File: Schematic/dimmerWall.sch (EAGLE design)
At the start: 22 parts, among them Q1 IRF840, T1 BC547

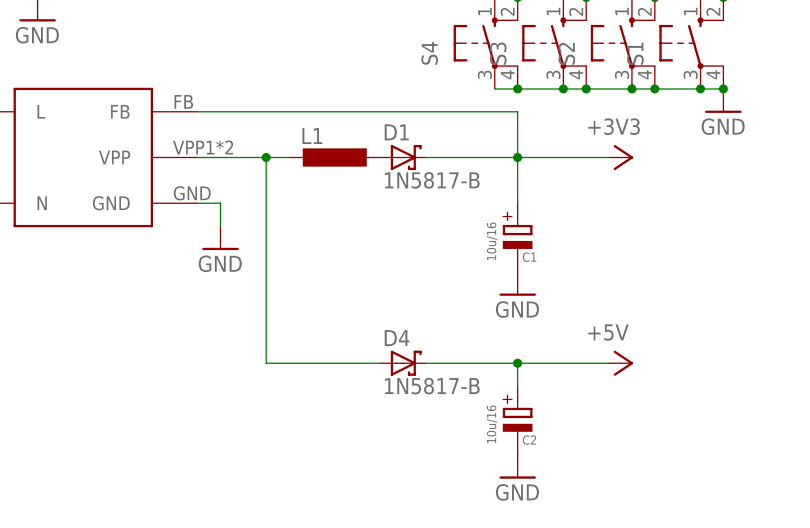
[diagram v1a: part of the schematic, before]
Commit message: Add L dimension
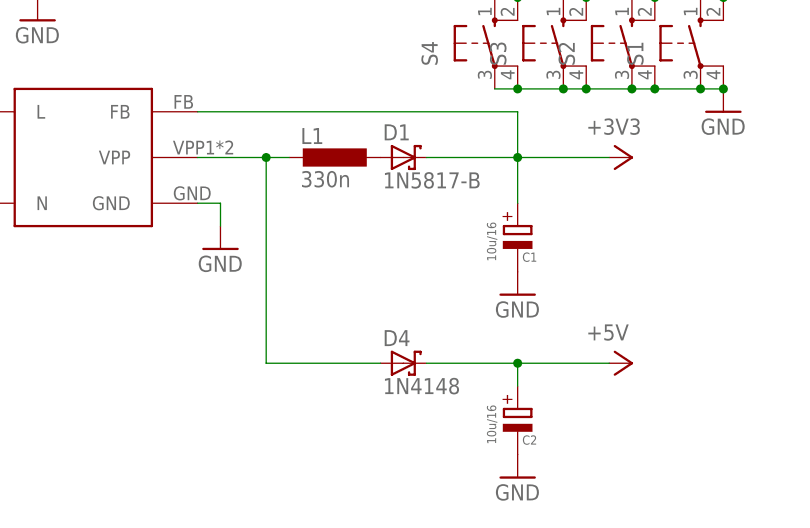
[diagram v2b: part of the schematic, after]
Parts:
- D4: value 1N5817-B -> 1N4148
- L1: value (none) -> 330n
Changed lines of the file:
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@@
 <part name="GND7" library="supply1" deviceset="GND" device=""/>
 <part name="GND9" library="supply1" deviceset="GND" device=""/>
-<part name="L1" library="rcl" deviceset="L-EU" device="0204/5"/>
+<part name="L1" library="rcl" deviceset="L-EU" device="0204/5" value="330n"/>
 <part name="P+1" library="supply1" deviceset="+5V" device=""/>
 <part name="U$1" library="esp8266modules" deviceset="ESP8266" device=""/>
@@
 <part name="GND6" library="supply1" deviceset="GND" device=""/>
 <part name="D1" library="diode" deviceset="1N581*" device="" technology="7-B"/>
-<part name="D4" library="diode" deviceset="1N581*" device="" technology="7-B"/>
+<part name="D4" library="diode" deviceset="1N581*" device="" technology="7-B" value="1N4148"/>
 <part name="F3" library="fuse" deviceset="FUSE" device="SHK20L" value="1A flink"/>
 <part name="S1" library="switch-omron" deviceset="10-XX" device=""/>

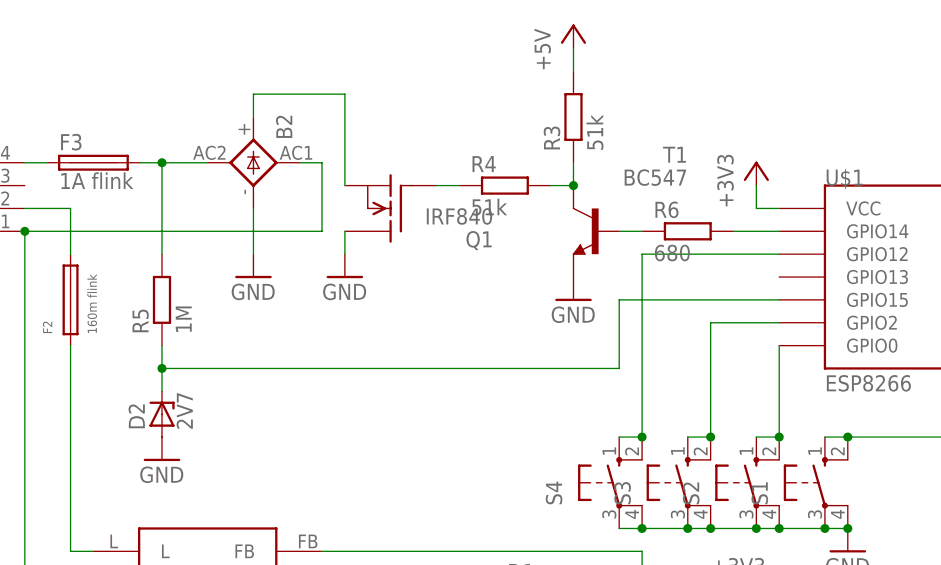
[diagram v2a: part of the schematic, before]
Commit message: Make board less higher
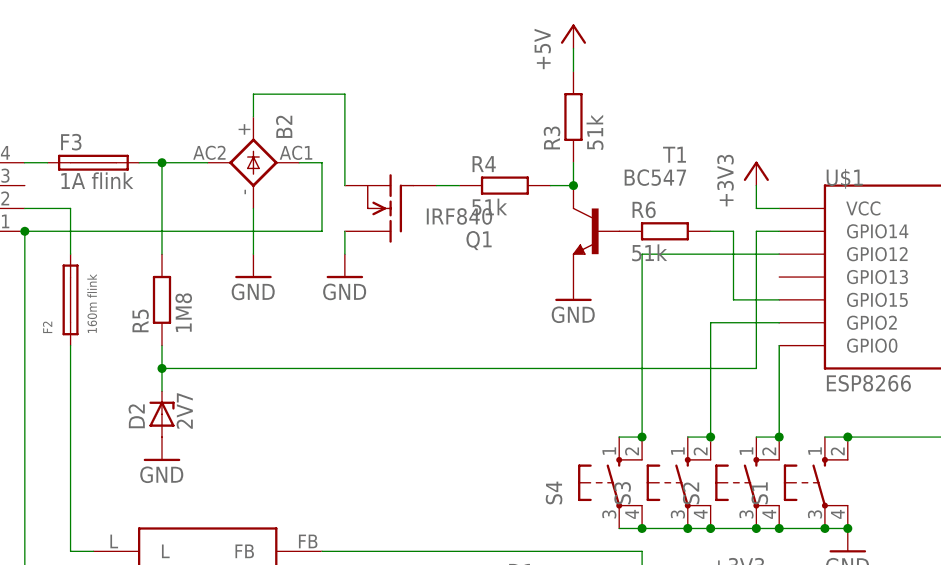
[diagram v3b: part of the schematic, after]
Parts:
- R3: device rcl:R-EU_0204/5 -> rcl:R-EU_0207/12
- R4: device rcl:R-EU_0207/10 -> rcl:R-EU_0207/12
- R5: value 1M -> 1M8
- R6: value 680 -> 51k; device rcl:R-EU_0204/7 -> rcl:R-EU_0207/12
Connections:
- removed net N$12: R6.2, U$1.GPIO14
- new net N$10: R6.2, U$1.GPIO15
- net N$7: now also U$1.GPIO14; no longer U$1.GPIO15
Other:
- moved on the sheet: R6
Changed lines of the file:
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@@
 <part name="PWR" library="con-lstb" deviceset="MA04-1" device=""/>
 <part name="F2" library="fuse" deviceset="19560" device="" value="160m flink"/>
-<part name="R3" library="rcl" deviceset="R-EU_" device="0204/5" value="51k"/>
-<part name="R4" library="rcl" deviceset="R-EU_" device="0207/10" value="51k"/>
-<part name="R5" library="rcl" deviceset="R-EU_" device="0207/12" value="1M"/>
+<part name="R3" library="rcl" deviceset="R-EU_" device="0207/12" value="51k"/>
+<part name="R4" library="rcl" deviceset="R-EU_" device="0207/12" value="51k"/>
+<part name="R5" library="rcl" deviceset="R-EU_" device="0207/12" value="1M8"/>
 <part name="D2" library="diode" deviceset="ZENER-DIODE" device="DO34-7" value="2V7"/>
 <part name="GND4" library="supply1" deviceset="GND" device=""/>
-<part name="R6" library="rcl" deviceset="R-EU_" device="0204/7" value="680"/>
+<part name="R6" library="rcl" deviceset="R-EU_" device="0207/12" value="51k"/>
 <part name="B2" library="rectifier" deviceset="2KBP" device=""/>
 <part name="C1" library="rcl" deviceset="CPOL-EU" device="E2.5-6" value="10u/16"/>
@@
 <instance part="D2" gate="G$1" x="-116.84" y="38.1" rot="R90"/>
 <instance part="GND4" gate="1" x="-116.84" y="33.02"/>
-<instance part="R6" gate="G$1" x="-58.42" y="58.42"/>
+<instance part="R6" gate="G$1" x="-60.96" y="58.42"/>
 <instance part="B2" gate="1" x="-106.68" y="66.04" rot="MR90"/>
 <instance part="C1" gate="G$1" x="-63.5" y="10.16" smashed="yes">
@@
 </segment>
 </net>
-<net name="N$12" class="0">
-<segment>
-<pinref part="R6" gate="G$1" pin="2"/>
-<wire x1="-53.34" y1="58.42" x2="-48.26" y2="58.42" width="0.1524" layer="91"/>
-<pinref part="U$1" gate="G$1" pin="GPIO14"/>
-</segment>
-</net>
 <net name="N$6" class="0">
 <segment>
@@
 <pinref part="T1" gate="G$1" pin="B"/>
 <pinref part="R6" gate="G$1" pin="1"/>
-<wire x1="-63.5" y1="58.42" x2="-66.04" y2="58.42" width="0.1524" layer="91"/>
 </segment>
 </net>
@@
 <wire x1="-116.84" y1="40.64" x2="-116.84" y2="43.18" width="0.1524" layer="91"/>
 <wire x1="-116.84" y1="43.18" x2="-116.84" y2="45.72" width="0.1524" layer="91"/>
-<wire x1="-116.84" y1="43.18" x2="-66.04" y2="43.18" width="0.1524" layer="91"/>
+<wire x1="-116.84" y1="43.18" x2="-50.8" y2="43.18" width="0.1524" layer="91"/>
 <junction x="-116.84" y="43.18"/>
-<pinref part="U$1" gate="G$1" pin="GPIO15"/>
-<wire x1="-48.26" y1="50.8" x2="-66.04" y2="50.8" width="0.1524" layer="91"/>
-<wire x1="-66.04" y1="50.8" x2="-66.04" y2="43.18" width="0.1524" layer="91"/>
+<wire x1="-50.8" y1="43.18" x2="-50.8" y2="58.42" width="0.1524" layer="91"/>
+<pinref part="U$1" gate="G$1" pin="GPIO14"/>
+<wire x1="-50.8" y1="58.42" x2="-48.26" y2="58.42" width="0.1524" layer="91"/>
 </segment>
 </net>
@@
 </segment>
 </net>
+<net name="N$10" class="0">
+<segment>
+<pinref part="U$1" gate="G$1" pin="GPIO15"/>
+<wire x1="-48.26" y1="50.8" x2="-53.34" y2="50.8" width="0.1524" layer="91"/>
+<wire x1="-53.34" y1="50.8" x2="-53.34" y2="58.42" width="0.1524" layer="91"/>
+<pinref part="R6" gate="G$1" pin="2"/>
+<wire x1="-53.34" y1="58.42" x2="-55.88" y2="58.42" width="0.1524" layer="91"/>
+</segment>
+</net>

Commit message: Use better schematic
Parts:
- added PROG: (no value), con-lstb:MA03-1
- C1, C2: device rcl:CPOL-EUE2.5-6 -> rcl:CPOL-EUTT2D4L
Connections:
- new net N$11: PROG.1, U$1.UTXD
- new net N$12: PROG.2, U$1.URXD
- net GND: now also PROG.3
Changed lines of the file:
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@@
 <grid distance="0.1" unitdist="inch" unit="inch" style="lines" multiple="1" display="no" altdistance="0.01" altunitdist="inch" altunit="inch"/>
 <layers>
-<layer number="1" name="Top" color="4" fill="1" visible="no" active="no"/>
-<layer number="16" name="Bottom" color="1" fill="1" visible="no" active="no"/>
-<layer number="17" name="Pads" color="2" fill="1" visible="no" active="no"/>
-<layer number="18" name="Vias" color="2" fill="1" visible="no" active="no"/>
-<layer number="19" name="Unrouted" color="6" fill="1" visible="no" active="no"/>
-<layer number="20" name="Dimension" color="15" fill="1" visible="no" active="no"/>
-<layer number="21" name="tPlace" color="7" fill="1" visible="no" active="no"/>
-<layer number="22" name="bPlace" color="7" fill="1" visible="no" active="no"/>
-<layer number="23" name="tOrigins" color="15" fill="1" visible="no" active="no"/>
-<layer number="24" name="bOrigins" color="15" fill="1" visible="no" active="no"/>
-<layer number="25" name="tNames" color="7" fill="1" visible="no" active="no"/>
-<layer number="26" name="bNames" color="7" fill="1" visible="no" active="no"/>
-<layer number="27" name="tValues" color="7" fill="1" visible="no" active="no"/>
-<layer number="28" name="bValues" color="7" fill="1" visible="no" active="no"/>
+<layer number="1" name="Top" color="4" fill="1" visible="yes" active="no"/>
+<layer number="16" name="Bottom" color="1" fill="1" visible="yes" active="no"/>
+<layer number="17" name="Pads" color="2" fill="1" visible="yes" active="no"/>
+<layer number="18" name="Vias" color="2" fill="1" visible="yes" active="no"/>
+<layer number="19" name="Unrouted" color="6" fill="1" visible="yes" active="no"/>
+<layer number="20" name="Dimension" color="15" fill="1" visible="yes" active="no"/>
+<layer number="21" name="tPlace" color="7" fill="1" visible="yes" active="no"/>
+<layer number="22" name="bPlace" color="7" fill="1" visible="yes" active="no"/>
+<layer number="23" name="tOrigins" color="15" fill="1" visible="yes" active="no"/>
+<layer number="24" name="bOrigins" color="15" fill="1" visible="yes" active="no"/>
+<layer number="25" name="tNames" color="7" fill="1" visible="yes" active="no"/>
+<layer number="26" name="bNames" color="7" fill="1" visible="yes" active="no"/>
+<layer number="27" name="tValues" color="7" fill="1" visible="yes" active="no"/>
+<layer number="28" name="bValues" color="7" fill="1" visible="yes" active="no"/>
 <layer number="29" name="tStop" color="7" fill="3" visible="no" active="no"/>
 <layer number="30" name="bStop" color="7" fill="6" visible="no" active="no"/>
@@
 <layer number="35" name="tGlue" color="7" fill="4" visible="no" active="no"/>
 <layer number="36" name="bGlue" color="7" fill="5" visible="no" active="no"/>
-<layer number="37" name="tTest" color="7" fill="1" visible="no" active="no"/>
-<layer number="38" name="bTest" color="7" fill="1" visible="no" active="no"/>
+<layer number="37" name="tTest" color="7" fill="1" visible="yes" active="no"/>
+<layer number="38" name="bTest" color="7" fill="1" visible="yes" active="no"/>
 <layer number="39" name="tKeepout" color="4" fill="11" visible="no" active="no"/>
 <layer number="40" name="bKeepout" color="1" fill="11" visible="no" active="no"/>
@@
 <layer number="44" name="Drills" color="7" fill="1" visible="no" active="no"/>
 <layer number="45" name="Holes" color="7" fill="1" visible="no" active="no"/>
-<layer number="46" name="Milling" color="3" fill="1" visible="no" active="no"/>
-<layer number="47" name="Measures" color="7" fill="1" visible="no" active="no"/>
-<layer number="48" name="Document" color="7" fill="1" visible="no" active="no"/>
-<layer number="49" name="Reference" color="7" fill="1" visible="no" active="no"/>
-<layer number="51" name="tDocu" color="7" fill="1" visible="no" active="no"/>
-<layer number="52" name="bDocu" color="7" fill="1" visible="no" active="no"/>
+<layer number="46" name="Milling" color="3" fill="1" visible="yes" active="no"/>
+<layer number="47" name="Measures" color="7" fill="1" visible="yes" active="no"/>
+<layer number="48" name="Document" color="7" fill="1" visible="yes" active="no"/>
+<layer number="49" name="Reference" color="7" fill="1" visible="yes" active="no"/>
+<layer number="51" name="tDocu" color="7" fill="1" visible="yes" active="no"/>
+<layer number="52" name="bDocu" color="7" fill="1" visible="yes" active="no"/>
 <layer number="91" name="Nets" color="2" fill="1" visible="yes" active="yes"/>
 <layer number="92" name="Busses" color="1" fill="1" visible="yes" active="yes"/>
@@
 <part name="R6" library="rcl" deviceset="R-EU_" device="0207/12" value="51k"/>
 <part name="B2" library="rectifier" deviceset="2KBP" device=""/>
-<part name="C1" library="rcl" deviceset="CPOL-EU" device="E2.5-6" value="10u/16"/>
-<part name="C2" library="rcl" deviceset="CPOL-EU" device="E2.5-6" value="10u/16"/>
+<part name="C1" library="rcl" deviceset="CPOL-EU" device="TT2D4L" value="10u/16"/>
+<part name="C2" library="rcl" deviceset="CPOL-EU" device="TT2D4L" value="10u/16"/>
 <part name="GND7" library="supply1" deviceset="GND" device=""/>
 <part name="GND9" library="supply1" deviceset="GND" device=""/>
@@
 <part name="GND8" library="supply1" deviceset="GND" device=""/>
 <part name="U$2" library="smps" deviceset="SMPS" device=""/>
+<part name="PROG" library="con-lstb" deviceset="MA03-1" device=""/>
 </parts>
 <sheets>
@@
 <instance part="GND8" gate="1" x="-40.64" y="22.86"/>
 <instance part="U$2" gate="G$1" x="-111.76" y="17.78"/>
+<instance part="PROG" gate="G$1" x="10.16" y="48.26" rot="R180"/>
 </instances>
 <busses>
@@
 <wire x1="-12.7" y1="45.72" x2="-12.7" y2="43.18" width="0.1524" layer="91"/>
 <pinref part="U$1" gate="G$1" pin="GND"/>
+<junction x="-12.7" y="45.72"/>
+<pinref part="PROG" gate="G$1" pin="3"/>
+<wire x1="-12.7" y1="45.72" x2="2.54" y2="45.72" width="0.1524" layer="91"/>
 </segment>
 <segment>
@@
 </segment>
 </net>
+<net name="N$11" class="0">
+<segment>
+<pinref part="U$1" gate="G$1" pin="UTXD"/>
+<pinref part="PROG" gate="G$1" pin="1"/>
+<wire x1="-15.24" y1="50.8" x2="2.54" y2="50.8" width="0.1524" layer="91"/>
+</segment>
+</net>
+<net name="N$12" class="0">
+<segment>
+<pinref part="PROG" gate="G$1" pin="2"/>
+<wire x1="2.54" y1="48.26" x2="0" y2="48.26" width="0.1524" layer="91"/>
+<wire x1="0" y1="48.26" x2="0" y2="53.34" width="0.1524" layer="91"/>
+<pinref part="U$1" gate="G$1" pin="URXD"/>
+<wire x1="0" y1="53.34" x2="-15.24" y2="53.34" width="0.1524" layer="91"/>
+</segment>
+</net>

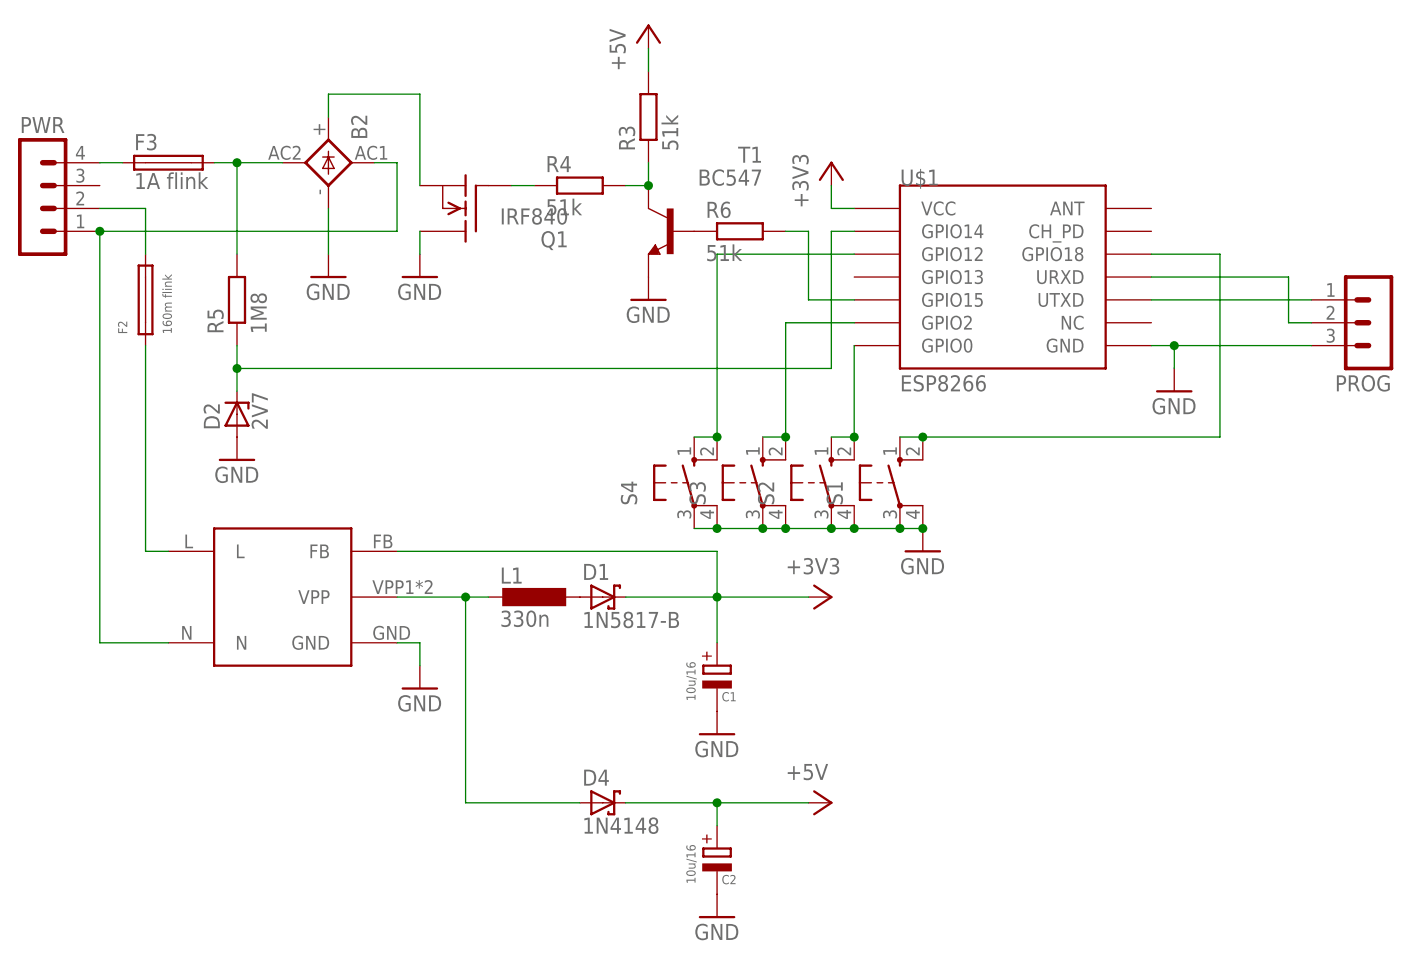
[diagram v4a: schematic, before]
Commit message: Connect correct pins for boot mode
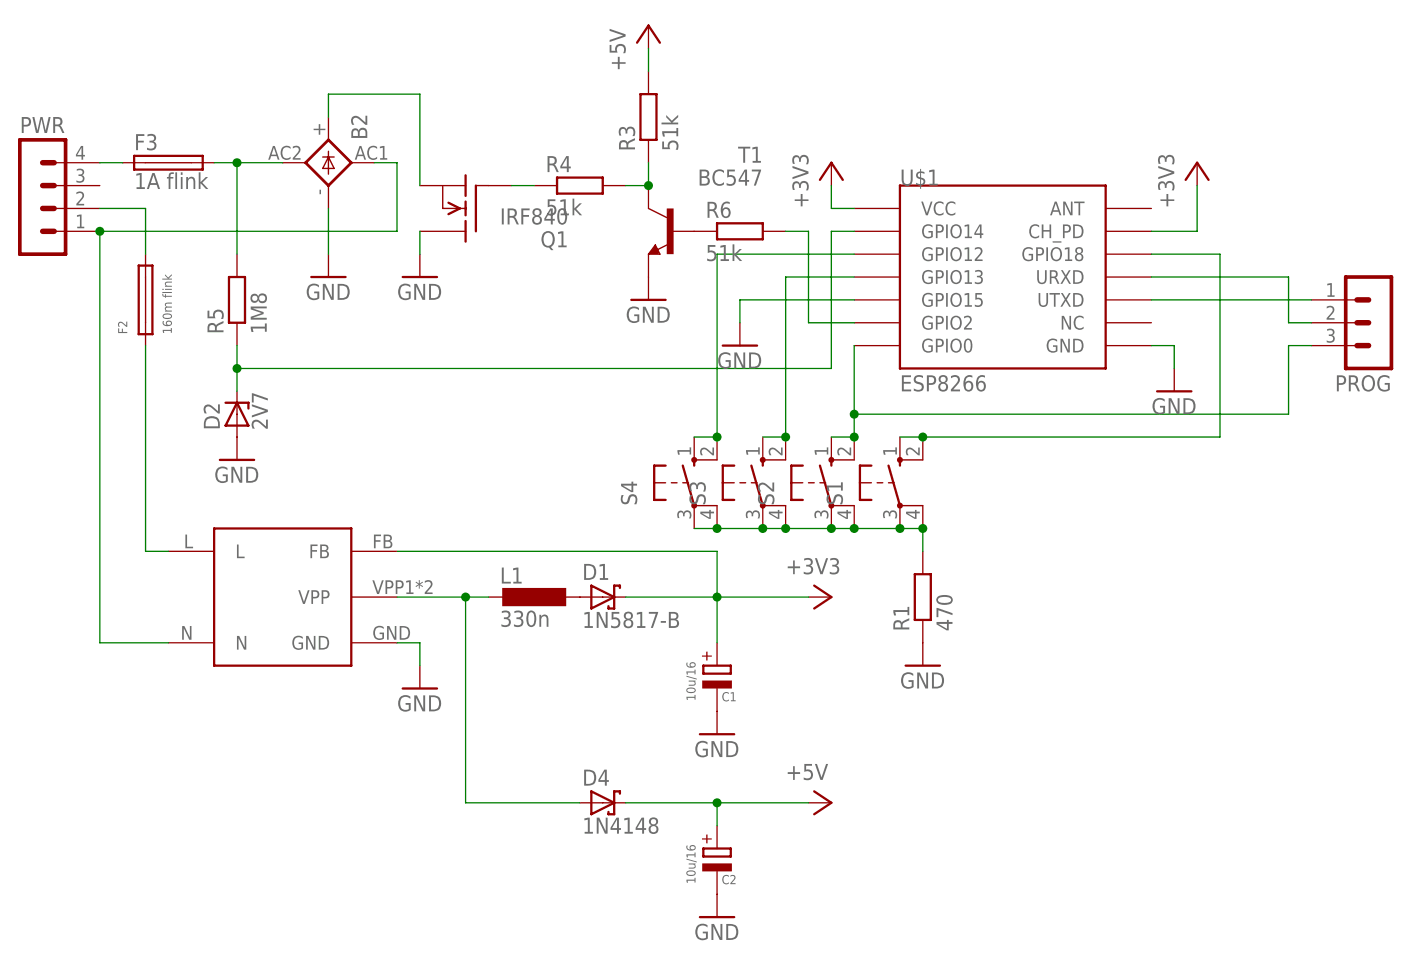
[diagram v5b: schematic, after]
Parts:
- added R1: 470, rcl:R-EU_0207/10
- R4: device rcl:R-EU_0207/12 -> rcl:R-EU_0204/7
- R6: device rcl:R-EU_0207/12 -> rcl:R-EU_0207/10
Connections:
- new net N$18: R1.2, S1.P, S1.P1, S2.P, S2.P1, S3.P, S3.P1, S4.P, S4.P1
- net +3V3: now also U$1.CH_PD
- net GND: now also R1.1, U$1.GPIO15; no longer PROG.3, S1.P, S1.P1, S2.P, S2.P1, S3.P, S3.P1, S4.P, S4.P1
- net N$10: now also U$1.GPIO2; no longer U$1.GPIO15
- net N$13: now also PROG.3
- net N$14: now also U$1.GPIO13; no longer U$1.GPIO2
